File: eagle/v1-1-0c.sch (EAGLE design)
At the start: 180 parts, among them J1 CR22A-44D-2.54DSA(70), J3 26-60-4040, J4 AUDIO_JACK_3.5MM_PTH, J5 DIN5, SW1 3PDT-AQ-SWITCH, SW2 9077-1, U10 7805, U11 74LS10N, U13 74LS04N, U14 4528N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

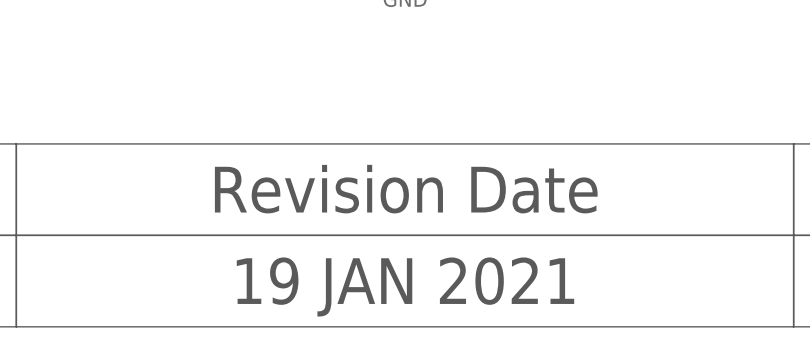
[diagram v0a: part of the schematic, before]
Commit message: Layout update
Fix a positioning problem with right cartridge port alignment/screw hole.
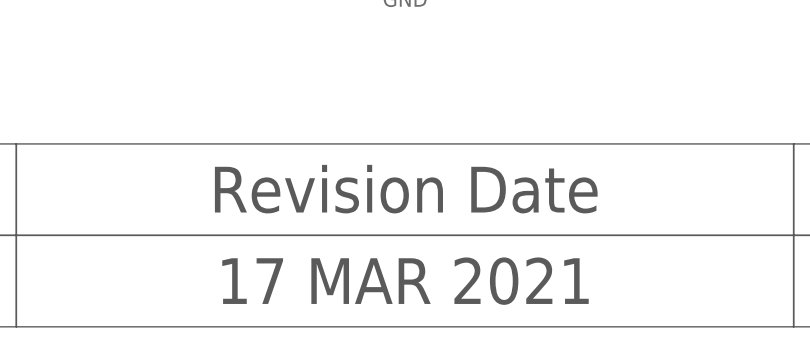
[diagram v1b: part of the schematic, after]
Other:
- note added: "17 MAR 2021"
- note removed: "19 JAN 2021"
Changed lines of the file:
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@@
 <wire x1="261.62" y1="15.24" x2="261.62" y2="5.08" width="0.1524" layer="97"/>
 <wire x1="261.62" y1="5.08" x2="347.98" y2="5.08" width="0.1524" layer="97"/>
-<text x="304.8" y="7.62" size="5.08" layer="97" align="bottom-center">19 JAN 2021</text>
+<text x="304.8" y="7.62" size="5.08" layer="97" align="bottom-center">17 MAR 2021</text>
 <wire x1="347.98" y1="15.24" x2="347.98" y2="25.4" width="0.1524" layer="97"/>
 <wire x1="347.98" y1="25.4" x2="261.62" y2="25.4" width="0.1524" layer="97"/>

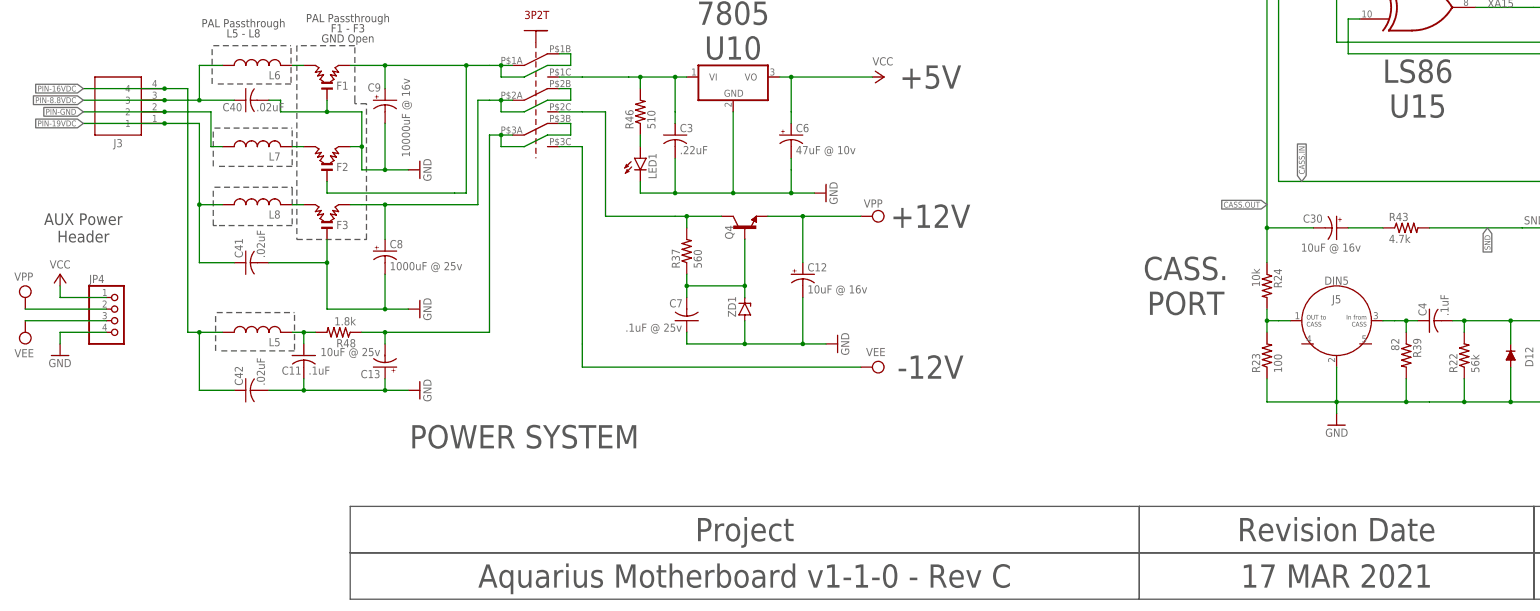
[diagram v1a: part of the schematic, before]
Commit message: Correct input voltages on PSU for schematic
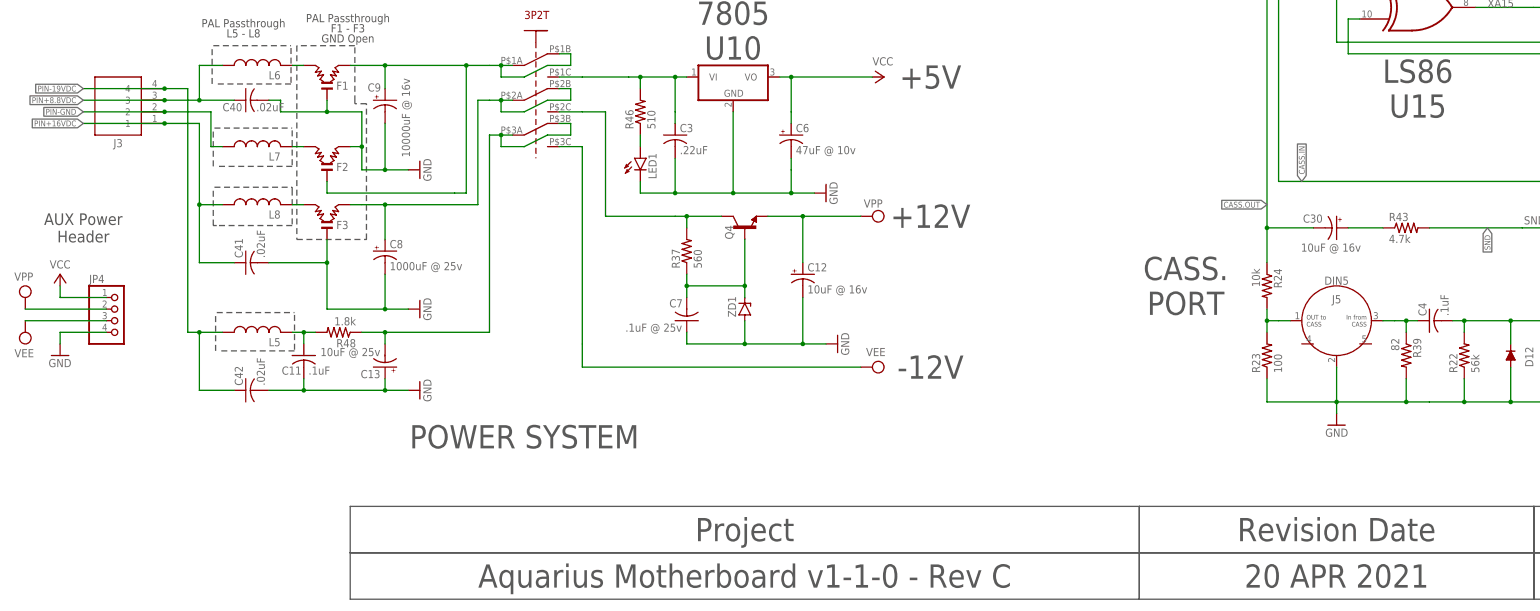
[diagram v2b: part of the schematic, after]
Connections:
- net PIN-8.8VDC renamed PIN+8.8VDC
- removed net PIN-16VDC: C42.1, J3.4, L5.1
- new net PIN+16VDC: C41.1, J3.1, L8.1
- net PIN-19VDC: now also C42.1, J3.4, L5.1; no longer C41.1, J3.1, L8.1
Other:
- note added: "20 APR 2021"
- note removed: "17 MAR 2021"
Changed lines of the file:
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@@
 <wire x1="261.62" y1="15.24" x2="261.62" y2="5.08" width="0.1524" layer="97"/>
 <wire x1="261.62" y1="5.08" x2="347.98" y2="5.08" width="0.1524" layer="97"/>
-<text x="304.8" y="7.62" size="5.08" layer="97" align="bottom-center">17 MAR 2021</text>
+<text x="304.8" y="7.62" size="5.08" layer="97" align="bottom-center">20 APR 2021</text>
 <wire x1="347.98" y1="15.24" x2="347.98" y2="25.4" width="0.1524" layer="97"/>
 <wire x1="347.98" y1="25.4" x2="261.62" y2="25.4" width="0.1524" layer="97"/>
@@
 </segment>
 </net>
-<net name="PIN-16VDC" class="0">
+<net name="PIN-19VDC" class="0">
 <segment>
 <pinref part="C42" gate="G$1" pin="1"/>
@@
 </segment>
 </net>
-<net name="PIN-8.8VDC" class="0">
+<net name="PIN+8.8VDC" class="0">
 <segment>
 <pinref part="C40" gate="G$1" pin="1"/>
@@
 </segment>
 </net>
-<net name="PIN-19VDC" class="0">
+<net name="PIN+16VDC" class="0">
 <segment>
 <pinref part="L8" gate="G$1" pin="1"/>
